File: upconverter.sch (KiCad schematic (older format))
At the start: 30 parts, among them J1 SMA_F, J2 SMA_F, J3 SMA_F, J4 USB_B_Mini, J5 SMA_F, U1 SBL-1, U2 SA602A, X1 XO32

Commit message: Updates to psu
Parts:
- removed R1: R, Resistor_THT:R_Axial_DIN0207_L6.3mm_D2.5mm_P10.16mm_Horizontal, symbol Device:R
- added C?: 220uF, symbol Device:CP1
- added C? (x2): 100nF, symbol Device:C
- added D?: 5v, symbol Device:LED
- added D?: 5v, symbol Device:D_Zener
- added D?: US1M, Diode_SMD:D_SMA, symbol Diode:US1M
- added D?: LED, symbol Device:LED
- added J?: Barrel_Jack, symbol Connector:Barrel_Jack
- added R? (x2): 1k, symbol Device:R
- added R?: 470R, symbol Device:R
- C10: value C -> 100nF
- C7: value CP1 -> 220uF
- D1: value D_Zener -> 3.3v
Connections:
- wire segments 68 -> 99
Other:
- note added: "Just spitballing on this cap -->"
- note added: "Note: Zener may cause psu noise\nin its attempt to regulate to 3.3v, \nhence the output cap. I don't think\nthe values are that critical"
- note added: "is 5v zener on the input\na good way to ensure\na high voltage like 12v\ndoesn't get put on the input?"
- moved on the sheet: C1, C10, C11, C12, C13, C2, C3, C4, C5, C6, C7, C8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

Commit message: Updated Schematic, removed SBL-1 version, added footprints, and started on layout.
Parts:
- removed C1, C13: 220nF, Capacitor_THT:CP_Radial_D5.0mm_P2.00mm, symbol Device:C
- removed C2: 100pF, Capacitor_THT:CP_Radial_D5.0mm_P2.00mm, symbol Device:C
- removed C3: 200pF, Capacitor_THT:CP_Radial_D5.0mm_P2.00mm, symbol Device:C
- removed D?: US1M, Diode_SMD:D_SMA, symbol Diode:US1M
- removed J1, J2: SMA_F, Connector_Coaxial:SMA_Amphenol_132289_EdgeMount, symbol Connector:Conn_Coaxial
- removed L1, L2: 400nH, Inductor_THT:L_Axial_L12.8mm_D5.8mm_P25.40mm_Horizontal_Fastron_HBCC, symbol Device:L
- removed U1: SBL-1, symbol ZAM-custom:SBL-1
- added D2: 1N4007, Diode_THT:D_DO-41_SOD81_P10.16mm_Horizontal, symbol Diode:1N4007
- C1, C3: renamed from C?; footprint (none) -> Capacitor_THT:C_Disc_D6.0mm_W2.5mm_P5.00mm
- C10: footprint Capacitor_THT:CP_Radial_D5.0mm_P2.00mm -> Capacitor_THT:C_Disc_D6.0mm_W2.5mm_P5.00mm
- C11, C12, C5: footprint Capacitor_THT:CP_Radial_D5.0mm_P2.00mm -> Capacitor_THT:C_Disc_D7.5mm_W4.4mm_P5.00mm
- C2: renamed from C?; footprint (none) -> Capacitor_THT:CP_Radial_D10.0mm_P5.00mm
- C4, C6, C9: footprint Capacitor_THT:CP_Radial_D5.0mm_P2.00mm -> Capacitor_THT:C_Disc_D3.0mm_W2.0mm_P2.50mm
- C7: footprint Capacitor_THT:CP_Radial_D5.0mm_P2.00mm -> Capacitor_THT:CP_Radial_D10.0mm_P5.00mm
- C8: value 200pF -> 100pF; footprint Capacitor_THT:CP_Radial_D5.0mm_P2.00mm -> Capacitor_THT:C_Disc_D3.0mm_W2.0mm_P2.50mm
- D3, D5: renamed from D?; footprint (none) -> LED_THT:LED_D5.0mm
- D4: renamed from D?; footprint (none) -> Diode_THT:D_5KPW_P7.62mm_Vertical_AnodeUp
- J1: renamed from J?; footprint (none) -> Connector_BarrelJack:BarrelJack_CUI_PJ-102AH_Horizontal
- J3, J5: footprint Connector_Coaxial:SMA_Amphenol_132289_EdgeMount -> Connector_Coaxial:SMA_Amphenol_901-144_Vertical
- R1, R5, R6: renamed from R?; footprint (none) -> Resistor_THT:R_Axial_DIN0207_L6.3mm_D2.5mm_P10.16mm_Horizontal
- U2: footprint (none) -> Package_SO:SO-8_3.9x4.9mm_P1.27mm; symbol ZAM-custom:SA602A -> upconverter-rescue:SA602A-ZAM-custom
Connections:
- wire segments 99 -> 75
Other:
- note removed: "Note: other's circuits may swap the IF and RF. -->\nThey're interchangeable"
- note removed: "SBL-1 version (incomplete)"
- note removed: "preferred NP0 or C0G ceramic caps for the LO"
- moved on the sheet: C1, C10, C11, C12, C3, C5, C6, C8, C9, J3, J5, L3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

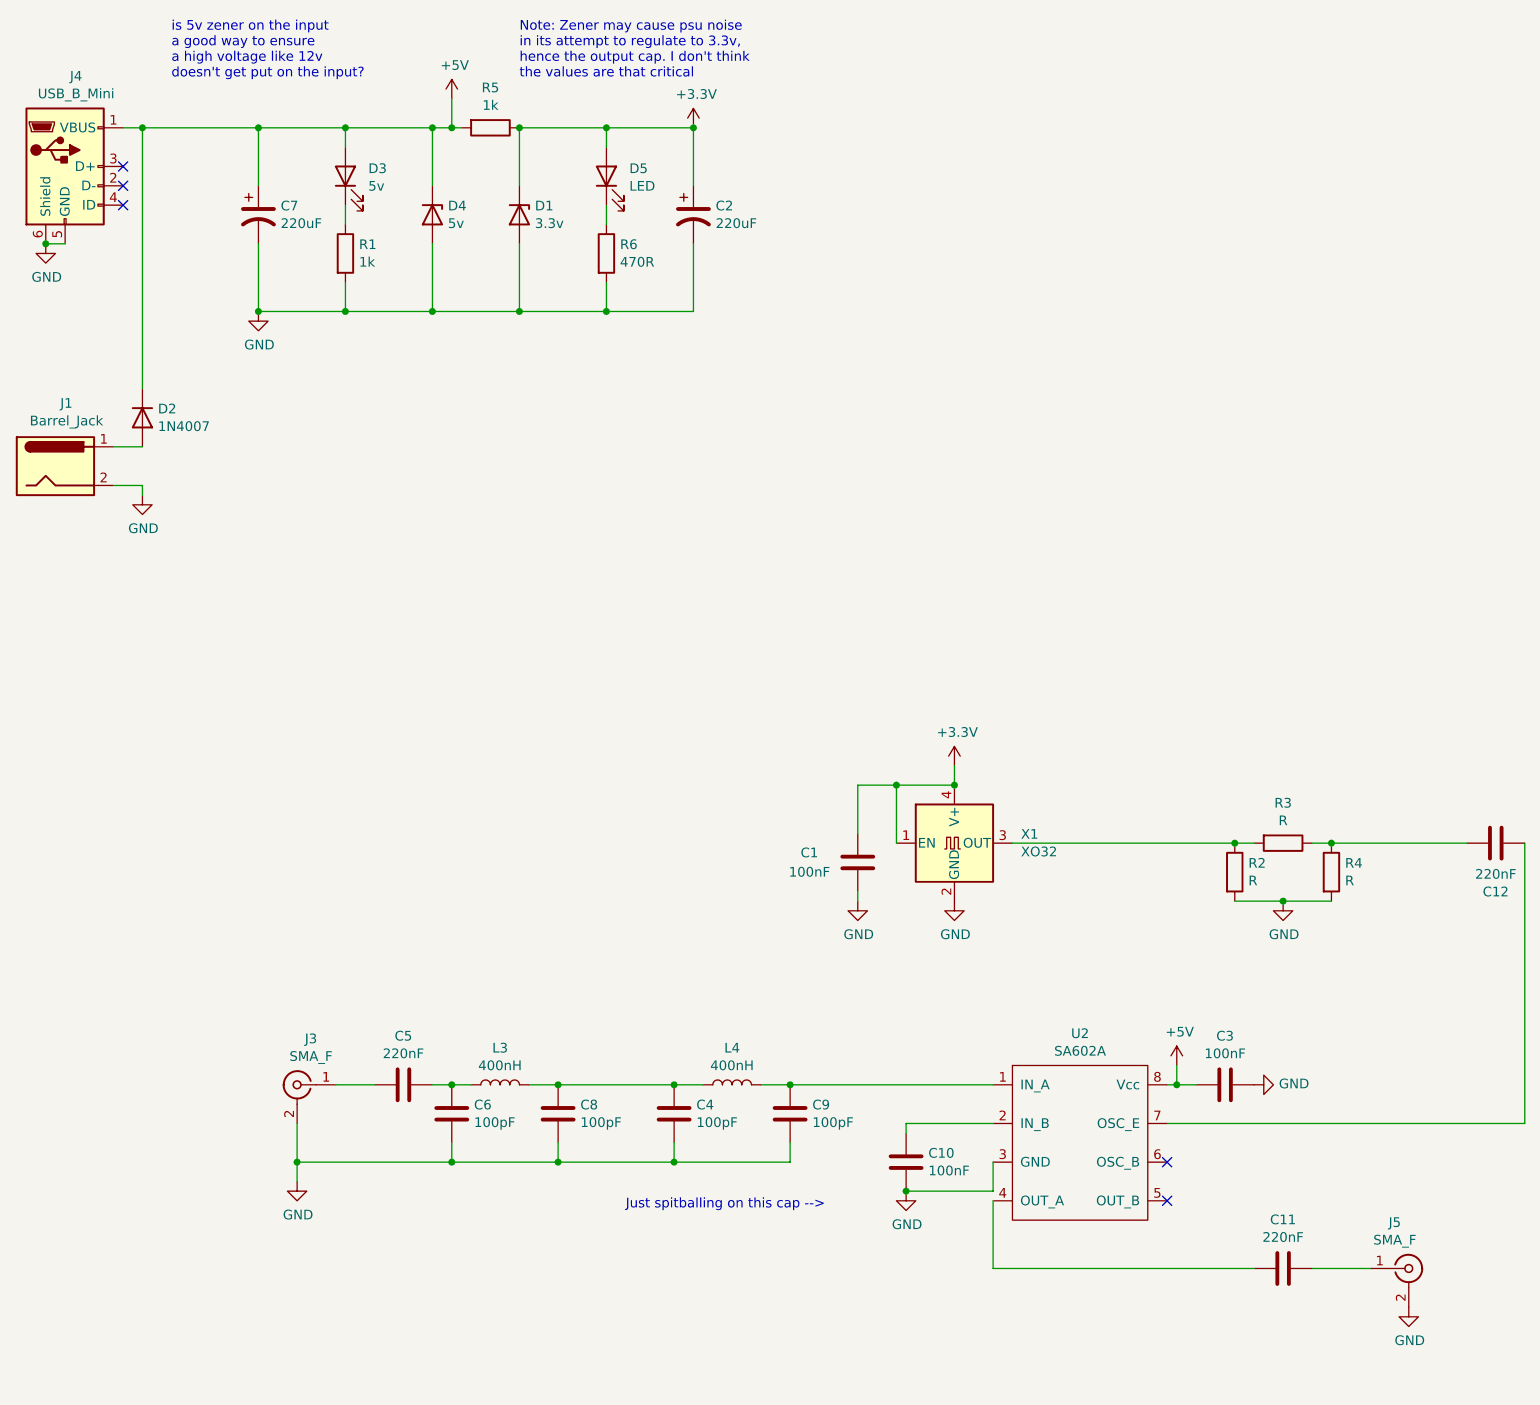
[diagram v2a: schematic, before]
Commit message: Changed filter, added matching xformers, changed power supplies to 7805 and 3.3v LDO
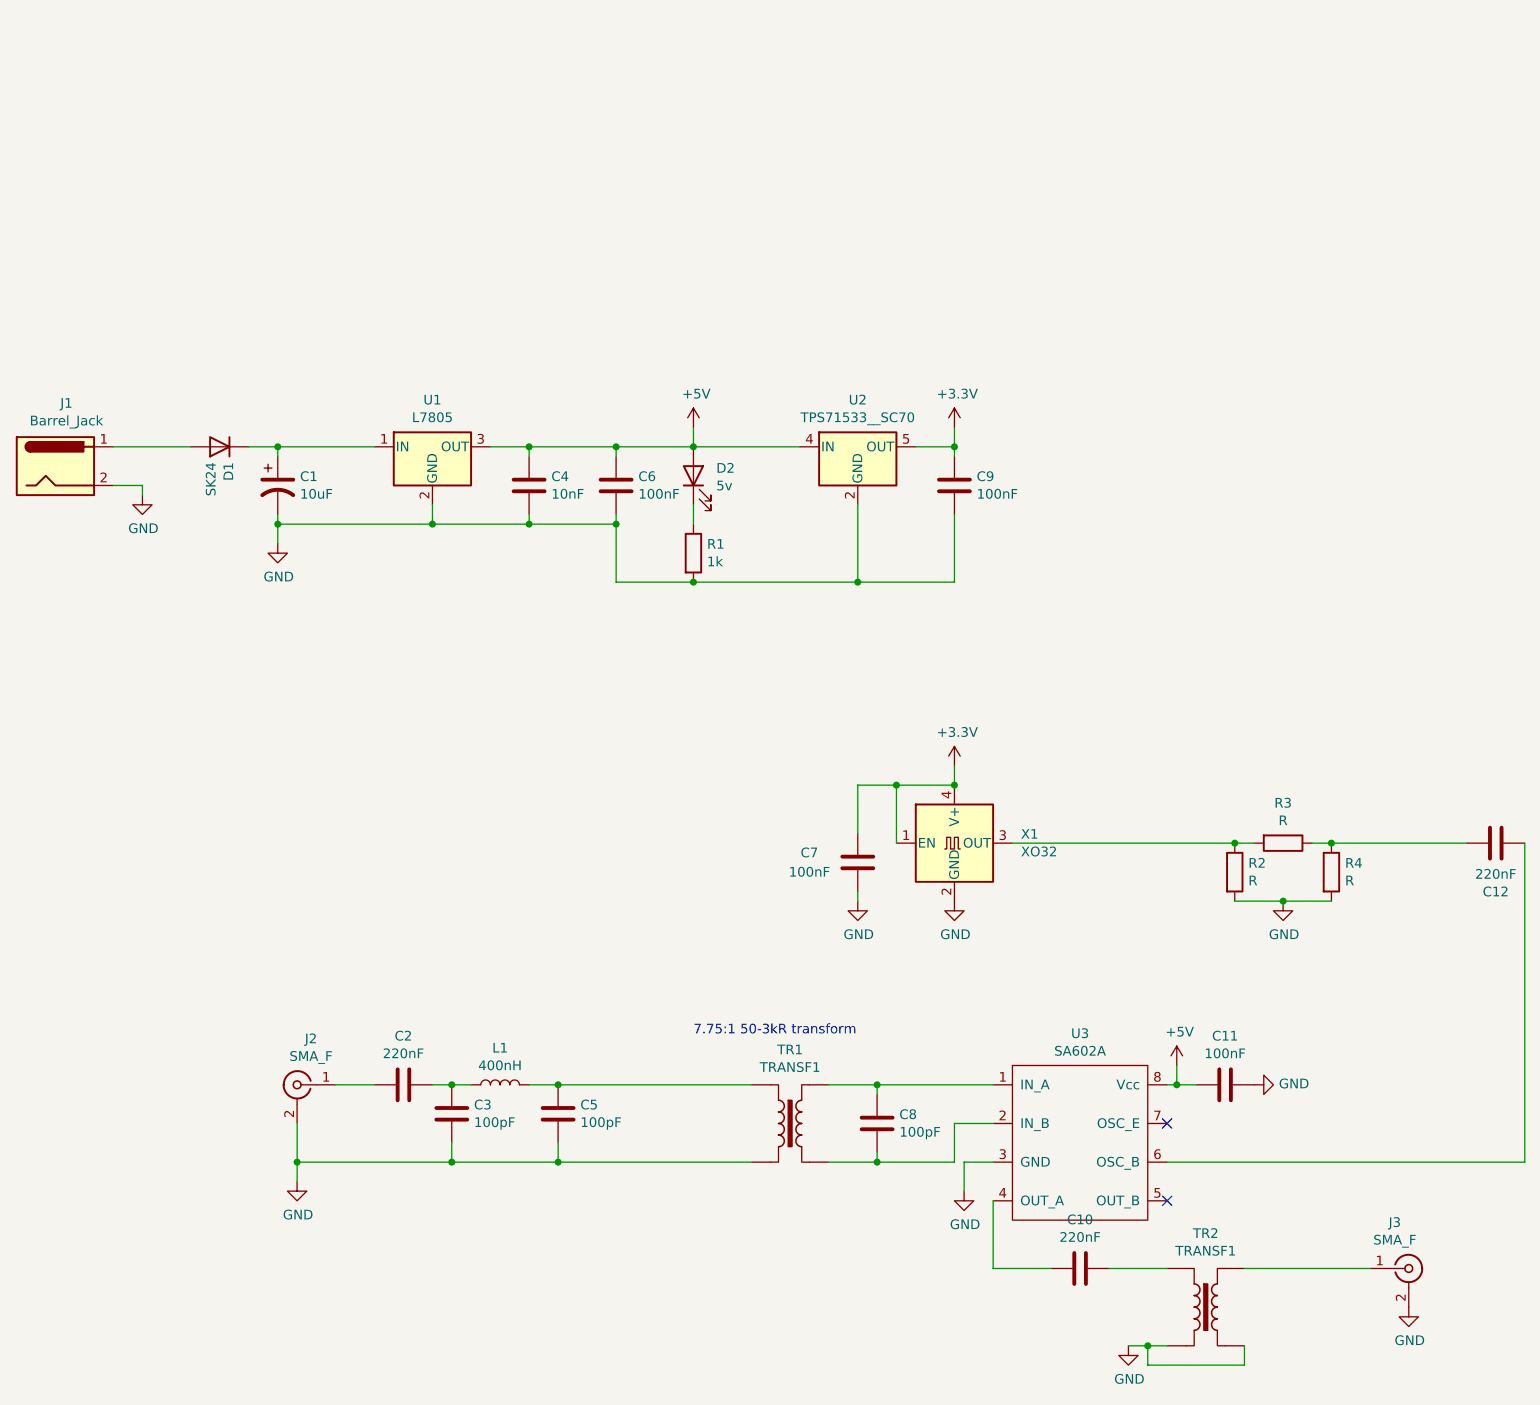
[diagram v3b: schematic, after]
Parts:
- removed C11: 220nF, Capacitor_THT:C_Disc_D7.5mm_W4.4mm_P5.00mm, symbol Device:C
- removed C2, C7: 220uF, Capacitor_THT:CP_Radial_D10.0mm_P5.00mm, symbol Device:CP1
- removed D1: 3.3v, Diode_THT:D_5KPW_P7.62mm_Vertical_AnodeUp, symbol Device:D_Zener
- removed D3: 5v, LED_THT:LED_D5.0mm, symbol Device:LED
- removed D4: 5v, Diode_THT:D_5KPW_P7.62mm_Vertical_AnodeUp, symbol Device:D_Zener
- removed D5: LED, LED_THT:LED_D5.0mm, symbol Device:LED
- removed J4: USB_B_Mini, Connector_USB:USB_Mini-B_Wuerth_65100516121_Horizontal, symbol Connector:USB_B_Mini
- removed L4: 400nH, Inductor_THT:L_Axial_L12.8mm_D5.8mm_P25.40mm_Horizontal_Fastron_HBCC, symbol Device:L
- removed R5: 1k, Resistor_THT:R_Axial_DIN0207_L6.3mm_D2.5mm_P10.16mm_Horizontal, symbol Device:R
- removed R6: 470R, Resistor_THT:R_Axial_DIN0207_L6.3mm_D2.5mm_P10.16mm_Horizontal, symbol Device:R
- added C1: 10uF, symbol Device:CP1
- added C10: 220nF, Capacitor_SMD:C_0805_2012Metric, symbol Device:C
- added C6: 100nF, Capacitor_SMD:C_0805_2012Metric, symbol Device:C
- added D2: 5v, symbol Device:LED
- added TR1, TR2: TRANSF1, symbol Transformer:TRANSF1
- added U1: L7805, symbol Regulator_Linear:L7805
- added U2: TPS71533__SC70, Package_TO_SOT_SMD:SOT-353_SC-70-5, symbol Regulator_Linear:TPS71533__SC70
- C11: renamed from C3; footprint Capacitor_THT:C_Disc_D6.0mm_W2.5mm_P5.00mm -> Capacitor_SMD:C_0805_2012Metric
- C12: footprint Capacitor_THT:C_Disc_D7.5mm_W4.4mm_P5.00mm -> Capacitor_SMD:C_0805_2012Metric
- C2: renamed from C5; footprint Capacitor_THT:C_Disc_D7.5mm_W4.4mm_P5.00mm -> Capacitor_SMD:C_0805_2012Metric
- C3: renamed from C6; footprint Capacitor_THT:C_Disc_D3.0mm_W2.0mm_P2.50mm -> Capacitor_SMD:C_0603_1608Metric
- C4: value 100pF -> 10nF; footprint Capacitor_THT:C_Disc_D3.0mm_W2.0mm_P2.50mm -> Capacitor_SMD:C_0805_2012Metric
- C5: renamed from C8; footprint Capacitor_THT:C_Disc_D3.0mm_W2.0mm_P2.50mm -> Capacitor_SMD:C_0603_1608Metric
- C7: renamed from C1; footprint Capacitor_THT:C_Disc_D6.0mm_W2.5mm_P5.00mm -> Capacitor_SMD:C_0805_2012Metric
- C8: renamed from C10; value 100nF -> 100pF; footprint Capacitor_THT:C_Disc_D6.0mm_W2.5mm_P5.00mm -> Capacitor_SMD:C_0603_1608Metric
- C9: value 100pF -> 100nF; footprint Capacitor_THT:C_Disc_D3.0mm_W2.0mm_P2.50mm -> Capacitor_SMD:C_0805_2012Metric
- D1: renamed from D2; value 1N4007 -> SK24; footprint Diode_THT:D_DO-41_SOD81_P10.16mm_Horizontal -> Diode_SMD:D_SMB
- J1: footprint Connector_BarrelJack:BarrelJack_CUI_PJ-102AH_Horizontal -> (none)
- J2: renamed from J3; footprint Connector_Coaxial:SMA_Amphenol_901-144_Vertical -> (none)
- J3: renamed from J5; footprint Connector_Coaxial:SMA_Amphenol_901-144_Vertical -> (none)
- L1: renamed from L3; footprint Inductor_THT:L_Axial_L12.8mm_D5.8mm_P25.40mm_Horizontal_Fastron_HBCC -> (none)
- R1: footprint Resistor_THT:R_Axial_DIN0207_L6.3mm_D2.5mm_P10.16mm_Horizontal -> Resistor_SMD:R_0805_2012Metric
- R2, R3, R4: footprint Resistor_THT:R_Axial_DIN0207_L6.3mm_D2.5mm_P10.16mm_Horizontal -> Resistor_SMD:R_0603_1608Metric
- X1: footprint Oscillator:Oscillator_SMD_EuroQuartz_XO32-4Pin_3.2x2.5mm -> (none)
- renumbered U2 to U3
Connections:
- net +3V3: now also C9.1, U2.5 (OUT)
- net +5V: now also C4.1, C6.1, D2.2 (A), U1.3 (OUT), U2.4 (IN); no longer D1.1 (K)
- net GND: now also C1.2, C6.2, TR1.2, TR2.2, TR2.3, U1.2 (GND), U2.2 (GND); no longer C8.2
- net at U3.1 (IN_A): now also C8.1, TR1.4; no longer C9.1
- net at U3.2 (IN_B): now also C8.2, TR1.3; no longer C8.1
- net at U3.4 (OUT_A): now also C10.2
- net at U3.6 (OSC_B): now also C12.2
- net at U3.7 (OSC_E): no longer C12.2
- net at C5.1, L1.2: now also TR1.1; no longer C4.1
- net at J3.1 (In): now also TR2.4
- net at R1.1: now also D2.1 (K)
- new net: C1.1, D1.1 (K), U1.1 (IN)
- new net: C10.1, TR2.1
- no-connect marks 5 -> 2
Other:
- note added: "7.75:1 50-3kR transform"
- note removed: "Just spitballing on this cap -->"
- note removed: "Note: Zener may cause psu noise\nin its attempt to regulate to 3.3v, \nhence the output cap. I don't think\nthe values are that critical"
- note removed: "is 5v zener on the input\na good way to ensure\na high voltage like 12v\ndoesn't get put on the input?"
- moved on the sheet: C8, D1

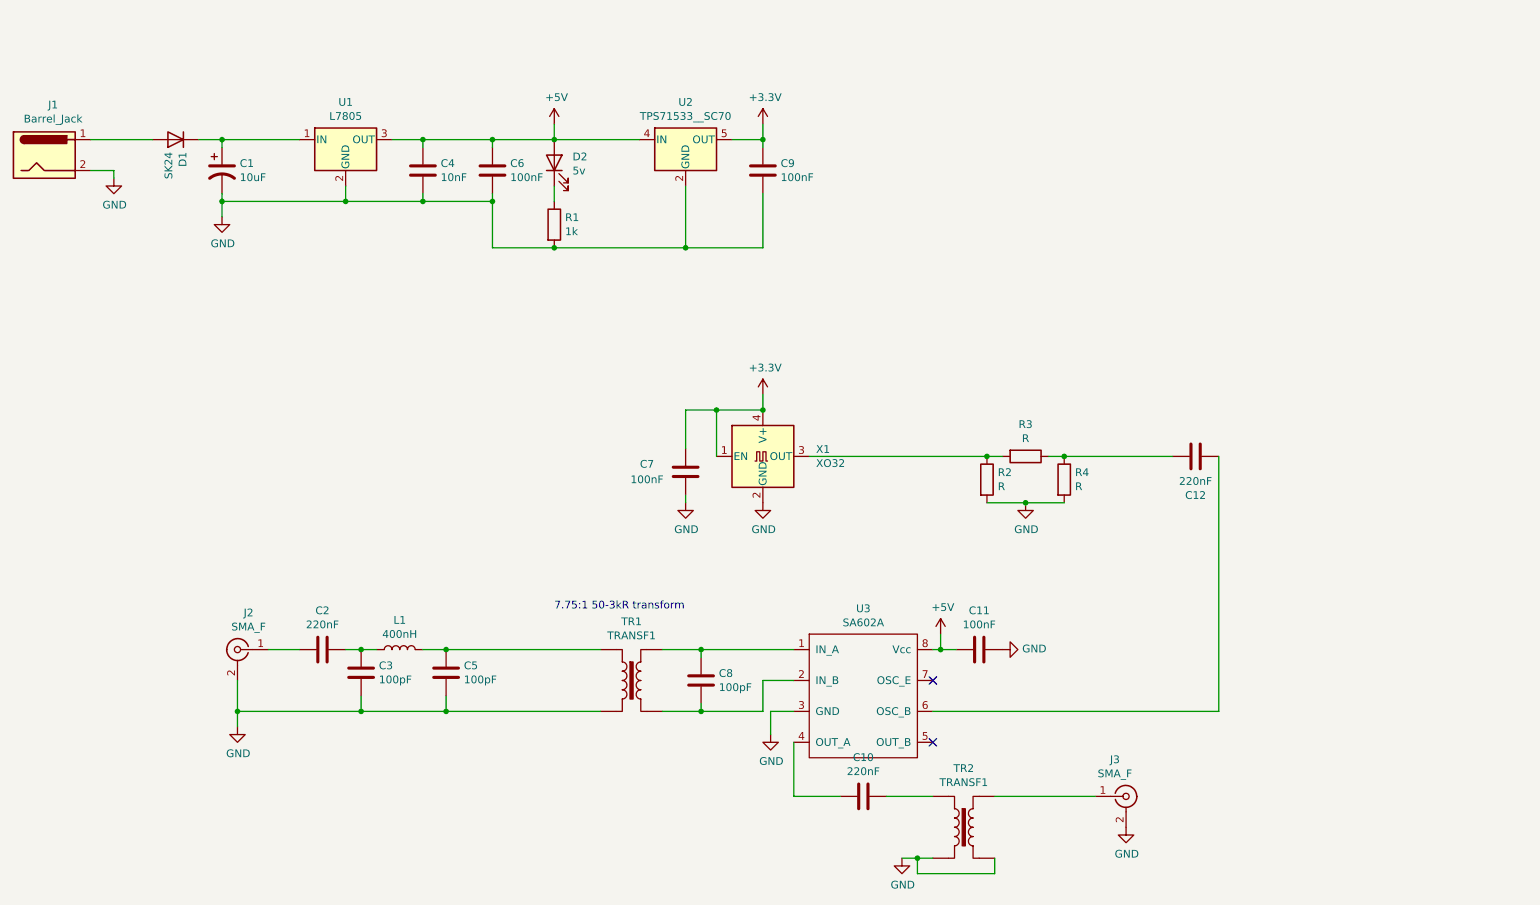
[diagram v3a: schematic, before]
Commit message: Updated footprints, transformer
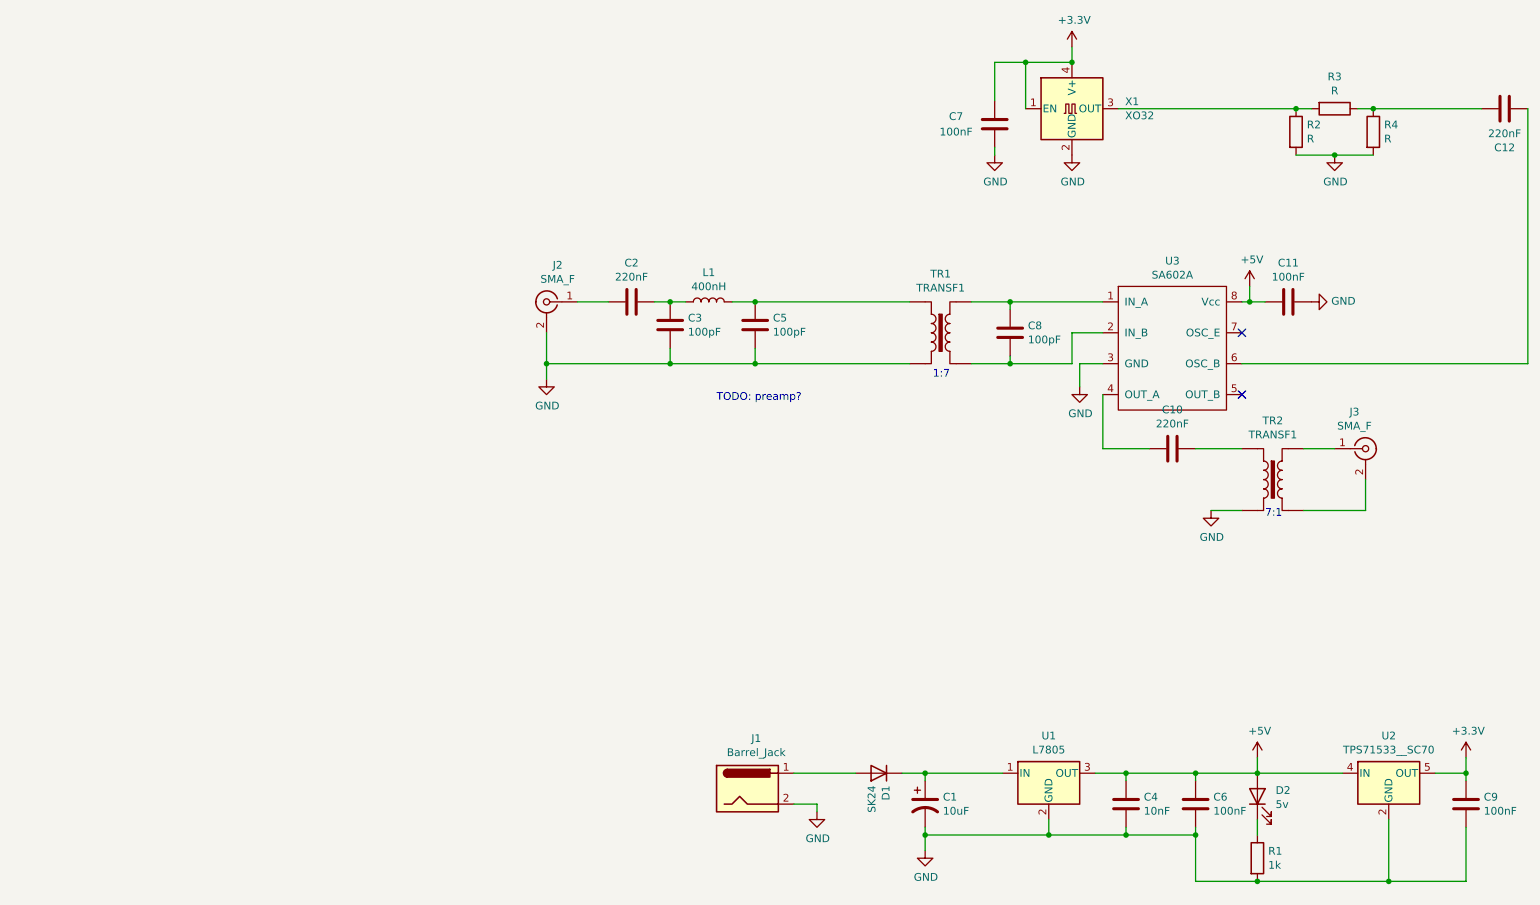
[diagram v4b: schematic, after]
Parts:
- D2: footprint (none) -> LED_THT:LED_D3.0mm
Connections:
- net GND: no longer J3.2 (Ext), TR2.3
- new net: J3.2 (Ext), TR2.3
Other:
- note added: "1:7"
- note added: "7:1"
- note added: "TODO: preamp?"
- note removed: "7.75:1 50-3kR transform"
- moved on the sheet: C1, C10, C11, C12, C2, C3, C4, C5, C6, C7, C8, C9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
